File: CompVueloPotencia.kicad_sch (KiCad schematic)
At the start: 7 parts, among them J1 Conn_01x03, J2 Conn_01x02, SW1 Reset, SW2 SW_SPDT_312, SW3 SW_SPDT_312

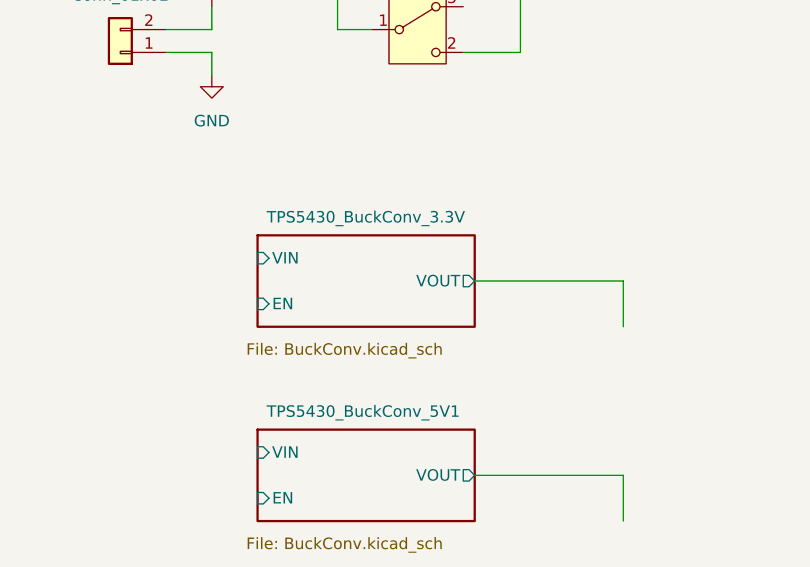
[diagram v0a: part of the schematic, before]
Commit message: Actualizacion de esquematicos de fuente tipo Buck
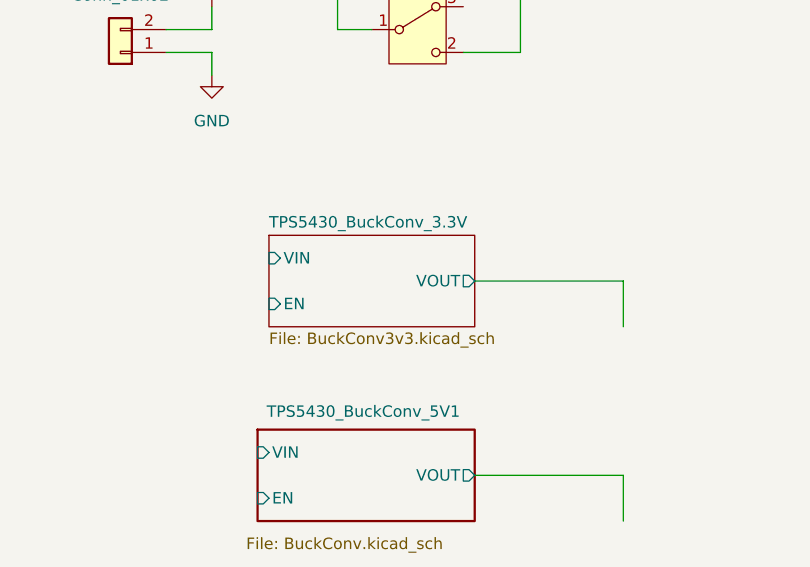
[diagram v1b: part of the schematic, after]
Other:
- sheet TPS5430_BuckConv_3.3V: file BuckConv.kicad_sch -> BuckConv3v3.kicad_sch
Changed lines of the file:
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@@
 	)
 	(sheet
-		(at 113.03 48.26)
-		(size 24.13 10.16)
-		(exclude_from_sim yes)
+		(at 114.3 48.26)
+		(size 22.86 10.16)
+		(exclude_from_sim no)
 		(in_bom yes)
 		(on_board yes)
 		(dnp no)
+		(fields_autoplaced yes)
 		(stroke
-			(width 0.254)
+			(width 0.1524)
 			(type solid)
 		)
@@
 		)
 		(property "Sheetname" "TPS5430_BuckConv_3.3V"
-			(at 114.046 46.99 0)
+			(at 114.3 47.5484 0)
 			(effects
 				(font
@@
 			)
 		)
-		(property "Sheetfile" "BuckConv.kicad_sch"
-			(at 111.76 60.198 0)
+		(property "Sheetfile" "BuckConv3v3.kicad_sch"
+			(at 114.3 59.0046 0)
 			(effects
 				(font
@@
 			)
 		)
+		(pin "EN" input
+			(at 114.3 55.88 180)
+			(effects
+				(font
+					(size 1.27 1.27)
+				)
+				(justify left)
+			)
+		)
 		(pin "VIN" input
-			(at 113.03 50.8 180)
+			(at 114.3 50.8 180)
 			(effects
 				(font
@@
 			)
 		)
-		(pin "EN" input
-			(at 113.03 55.88 180)
-			(effects
-				(font
-					(size 1.27 1.27)
-				)
-				(justify left)
-			)
-		)
 		(instances
 			(project "CompVueloPotencia"
 				(path "/a84aba9c-0fb9-4754-89f4-1b118d6ea201"
-					(page "2")
+					(page "4")
 				)
 			)

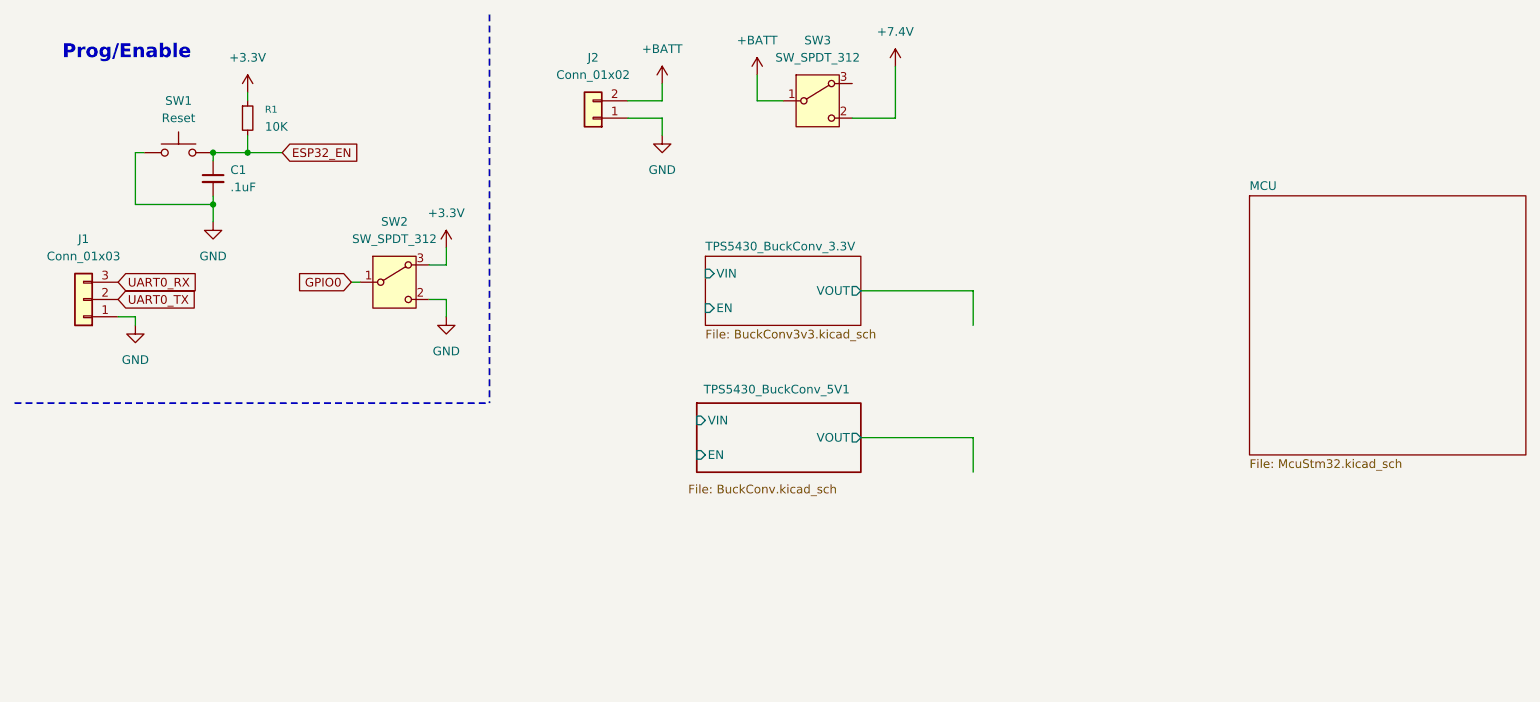
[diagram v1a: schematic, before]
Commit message: Semi finished the regulator-section
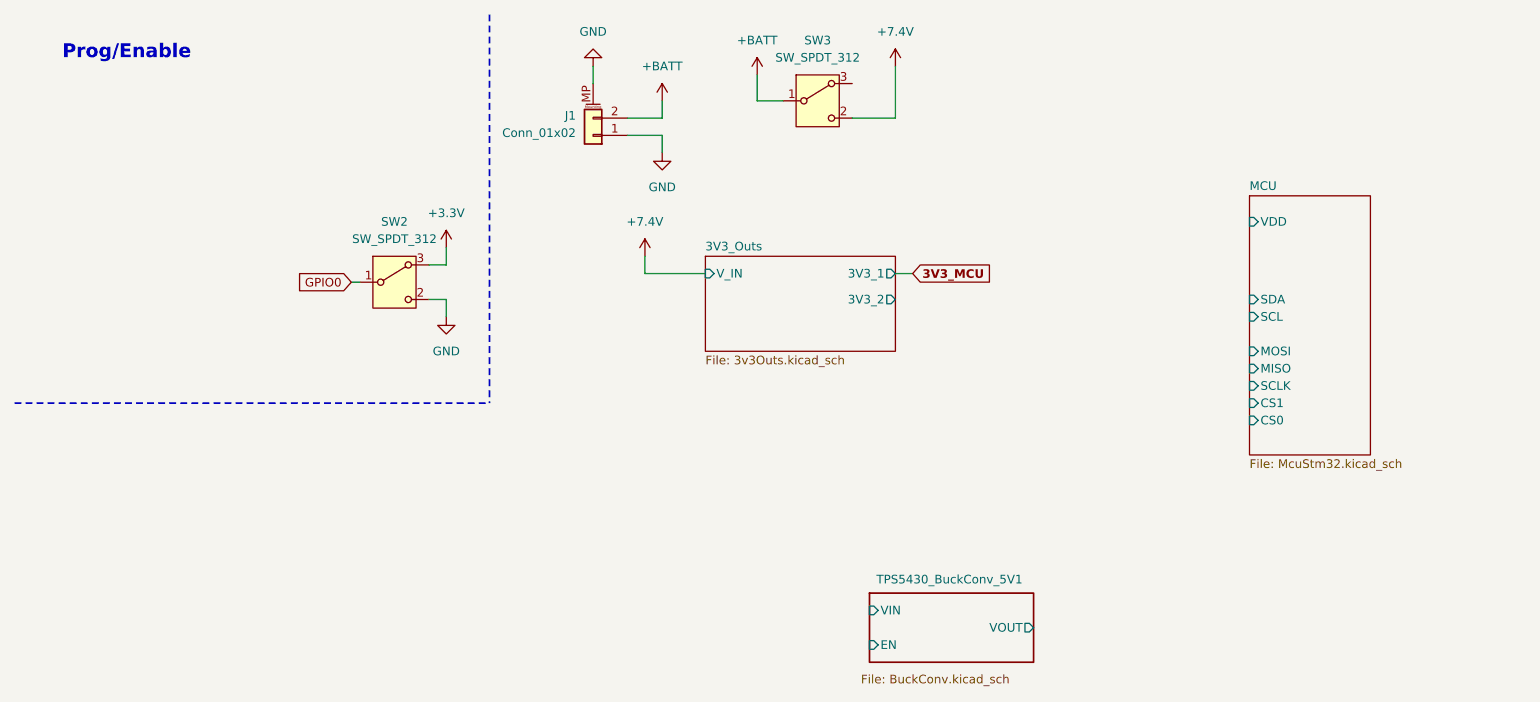
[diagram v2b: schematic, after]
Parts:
- removed C1: .1uF, symbol Device:C_Small
- removed J1: Conn_01x03, symbol Connector_Generic:Conn_01x03
- removed J2: Conn_01x02, Connector_JST:JST_PH_B2B-PH-SM4-TB_1x02-1MP_P2.00mm_Vertical, symbol Connector_Generic:Conn_01x02
- removed R1: 10K, symbol Device:R_Small
- removed SW1: Reset, Button_Switch_SMD:SW_SPST_SKQG_WithStem, symbol Switch:SW_Push
- added J1: Conn_01x02, Connector_JST:JST_PH_B2B-PH-SM4-TB_1x02-1MP_P2.00mm_Vertical, symbol Connector_Generic_MountingPin:Conn_01x02_MountingPin
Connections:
- net +BATT: now also J1.2 (Pin_2)
- net GND: now also J1.1 (Pin_1), J1.MP (MountPin)
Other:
- removed sheet TPS5430_BuckConv_3.3V
- added sheet 3V3_Outs (3v3Outs.kicad_sch)
- sheet MCU ports: added CS0, CS1, MISO, MOSI, SCL, SCLK, SDA, VDD; removed none
